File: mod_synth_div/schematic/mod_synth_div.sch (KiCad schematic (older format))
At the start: 68 parts, among them J1 In, J10 Conn_01x05_Female, J11 Conn_01x05_Male, J12 Conn_01x05_Female, J13 Conn_01x05_Male, J2 Rst, J3 Conn_02x08_Odd_Even, J4 1/2, J5 1/4, J6 1/8, J7 1/16, J8 1/32, J9 1/1, Q1 BC550, Q10 BC550, Q11 BC550, Q2 BC550, Q3 BC550, Q4 BC550, Q5 BC550, Q6 BC550, Q7 BC550, Q8 BC550, Q9 BC550, U1 4024

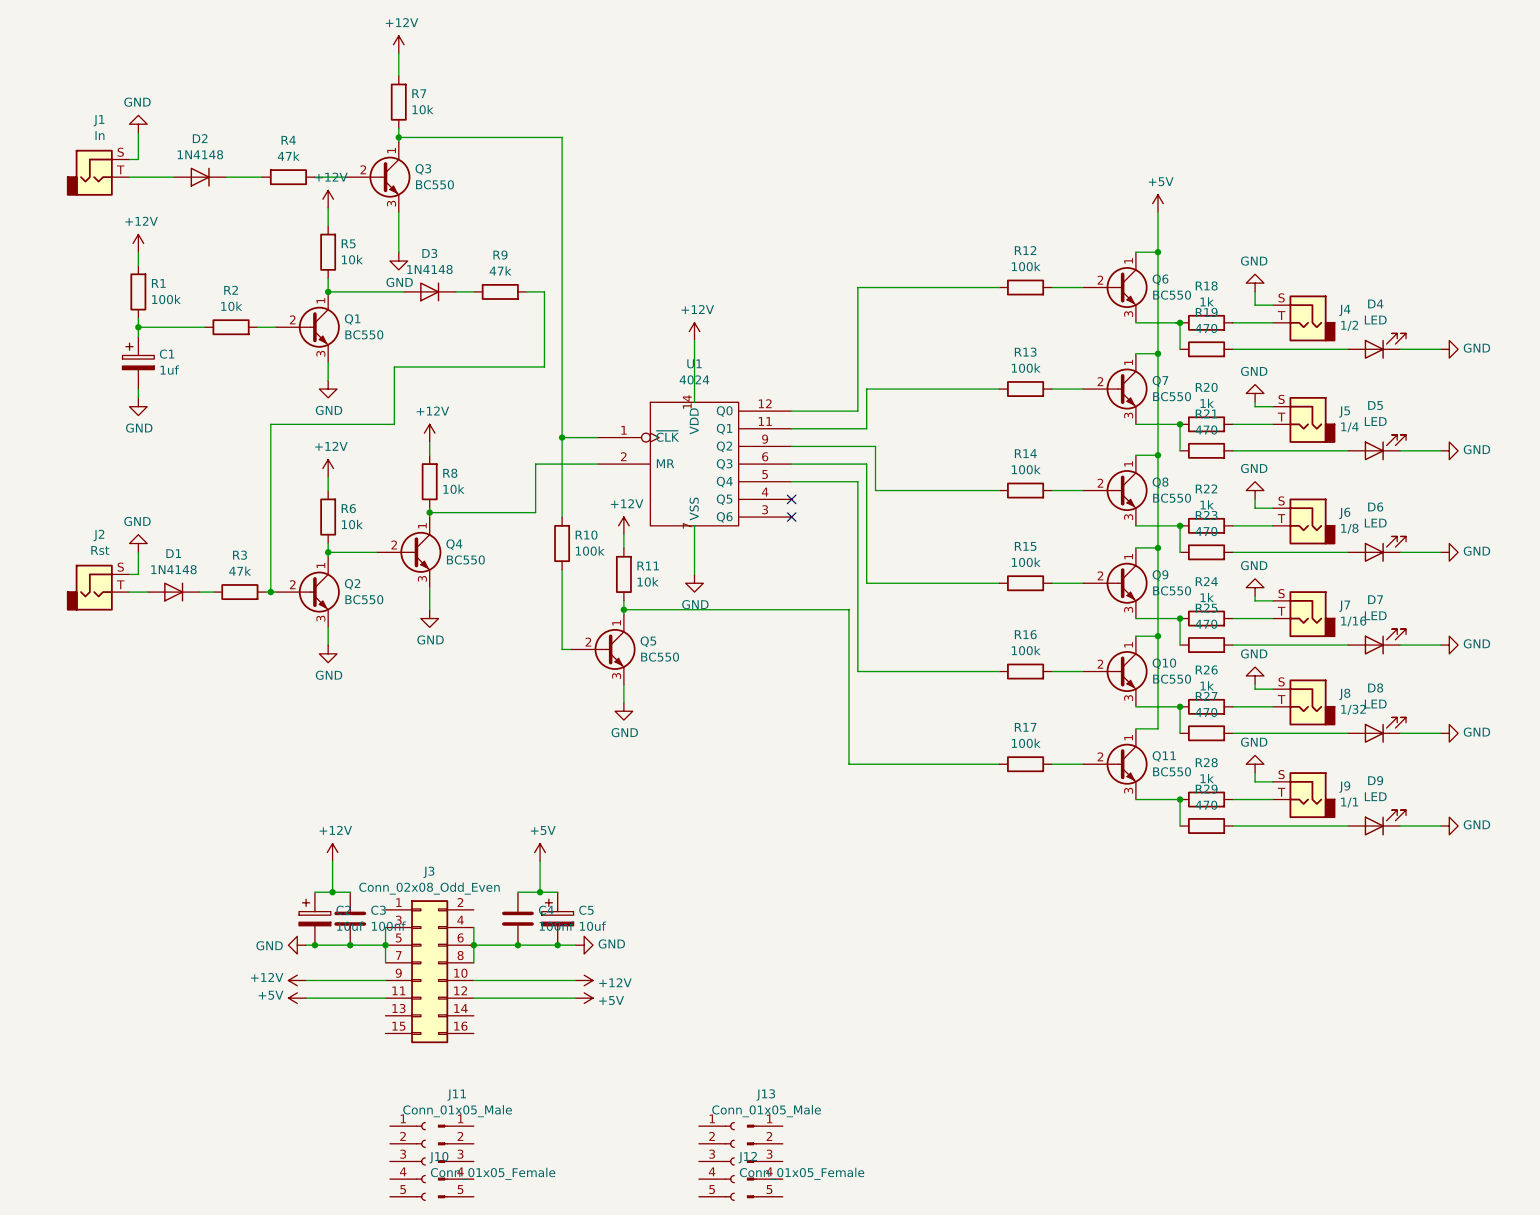
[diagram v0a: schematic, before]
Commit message: Add PCB connectors
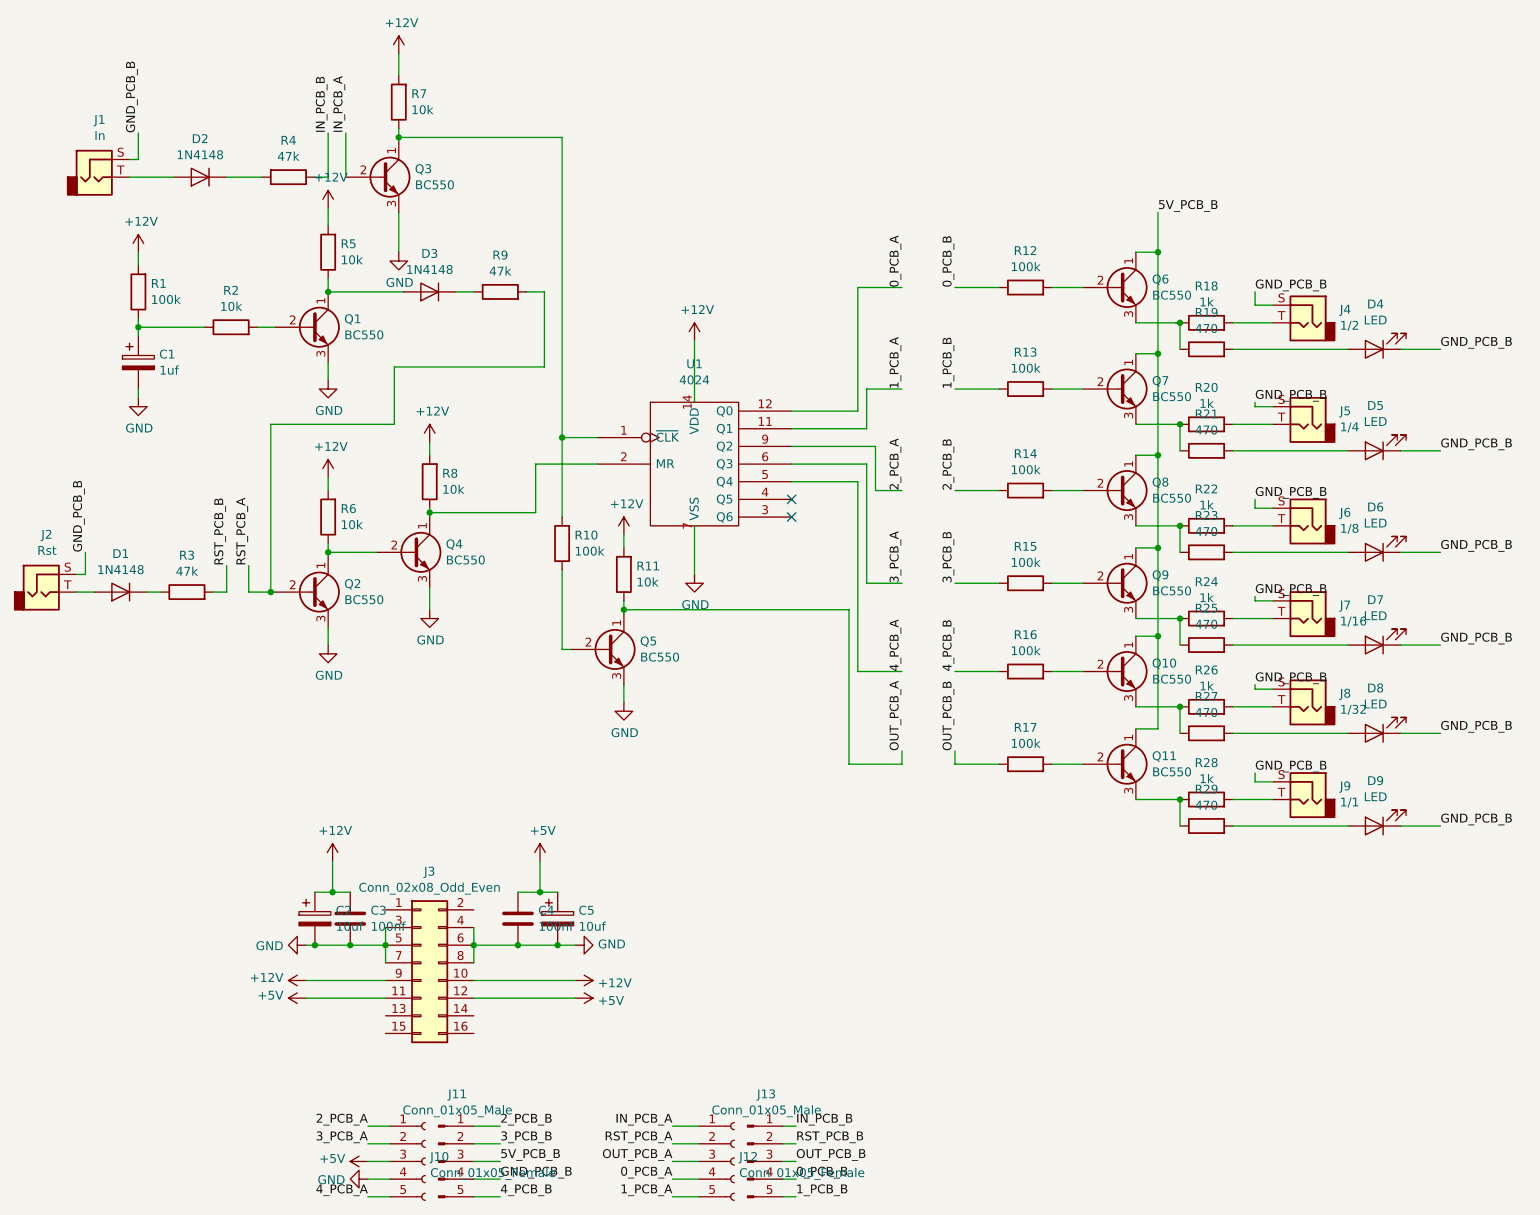
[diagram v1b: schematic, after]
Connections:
- net +5V: now also J10.3 (Pin_3); no longer Q10.1 (C), Q11.1 (C), Q6.1 (C), Q7.1 (C), Q8.1 (C), Q9.1 (C)
- net GND: now also J10.4 (Pin_4); no longer D4.1 (K), D5.1 (K), D6.1 (K), D7.1 (K), D8.1 (K), D9.1 (K), J1.S, J2.S, J4.S, J5.S, J6.S, J7.S, J8.S, J9.S
- net 1_PCB_A: now reaches U1.11 (Q1)
- net 1_PCB_A: now also J12.5 (Pin_5); no longer R13.1
- net 0_PCB_A: now reaches U1.12 (Q0)
- net 0_PCB_A: now also J12.4 (Pin_4); no longer R12.1
- net 4_PCB_A: now reaches U1.5 (Q4)
- net 4_PCB_A: now also J10.5 (Pin_5); no longer R16.1
- net 3_PCB_A: now reaches U1.6 (Q3)
- net 3_PCB_A: now also J10.2 (Pin_2); no longer R15.1
- net 2_PCB_A: now reaches U1.9 (Q2)
- net 2_PCB_A: now also J10.1 (Pin_1); no longer R14.1
- net IN_PCB_A: now reaches Q3.2 (B)
- net IN_PCB_A: now also J12.1 (Pin_1); no longer R4.1
- net OUT_PCB_A: now reaches Q5.1 (C), R11.1
- net OUT_PCB_A: now also J12.3 (Pin_3); no longer R17.1
- net RST_PCB_A: now reaches Q2.2 (B), R9.2
- net RST_PCB_A: now also J12.2 (Pin_2); no longer R3.2
- net 2_PCB_B: now reaches J11.1 (Pin_1)
- net 2_PCB_B: now also R14.1
- net 3_PCB_B: now reaches J11.2 (Pin_2)
- net 3_PCB_B: now also R15.1
- net 5V_PCB_B: now reaches J11.3 (Pin_3)
- net 5V_PCB_B: now also Q10.1 (C), Q11.1 (C), Q6.1 (C), Q7.1 (C), Q8.1 (C), Q9.1 (C)
- net GND_PCB_B: now reaches J11.4 (Pin_4)
- net GND_PCB_B: now also D4.1 (K), D5.1 (K), D6.1 (K), D7.1 (K), D8.1 (K), D9.1 (K), J1.S, J2.S, J4.S, J5.S, J6.S, J7.S, J8.S, J9.S
- net 4_PCB_B: now reaches J11.5 (Pin_5)
- net 4_PCB_B: now also R16.1
- net IN_PCB_B: now reaches J13.1 (Pin_1)
- net IN_PCB_B: now also R4.1
- net RST_PCB_B: now reaches J13.2 (Pin_2)
- net RST_PCB_B: now also R3.2
- net OUT_PCB_B: now reaches J13.3 (Pin_3)
- net OUT_PCB_B: now also R17.1
- net 0_PCB_B: now reaches J13.4 (Pin_4)
- net 0_PCB_B: now also R12.1
- net 1_PCB_B: now reaches J13.5 (Pin_5)
- net 1_PCB_B: now also R13.1
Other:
- moved on the sheet: D1, J2, R3

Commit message: Use correct size socket
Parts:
- U1: footprint Package_DIP:DIP-16_W7.62mm_Socket_LongPads -> Package_DIP:DIP-14_W7.62mm_Socket_LongPads
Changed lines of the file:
@@
 EESchema Schematic File Version 4
+LIBS:mod_synth_div-cache
 EELAYER 29 0
 EELAYER END
@@
 F 0 "U1" H 4600 3816 50  0000 C CNN
 F 1 "4024" H 4600 3725 50  0000 C CNN
-F 2 "Package_DIP:DIP-16_W7.62mm_Socket_LongPads" H 4600 3200 50  0001 C CNN
+F 2 "Package_DIP:DIP-14_W7.62mm_Socket_LongPads" H 4600 3200 50  0001 C CNN
 F 3 "" H 4600 3200 50  0001 C CNN
 	1    4600 3200
